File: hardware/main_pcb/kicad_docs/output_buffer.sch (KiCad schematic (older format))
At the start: 4 parts, among them U1 TL072

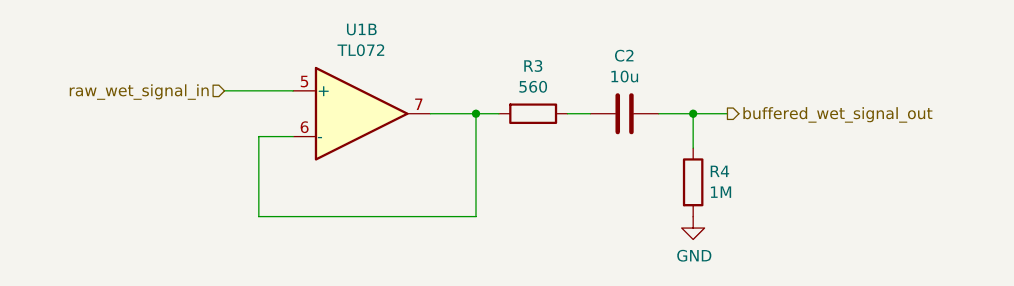
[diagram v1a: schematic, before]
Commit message: flip env invert switch, condense cap types
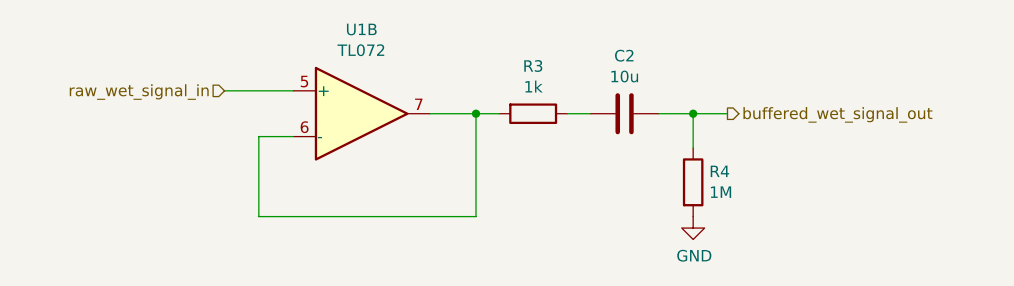
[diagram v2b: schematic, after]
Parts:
- R3: value 560 -> 1k
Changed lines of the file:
@@
 P 6300 3750
 F 0 "R3" V 6093 3750 50  0000 C CNN
-F 1 "560" V 6184 3750 50  0000 C CNN
+F 1 "1k" V 6184 3750 50  0000 C CNN
 F 2 "Resistor_SMD:R_0805_2012Metric" V 6230 3750 50  0001 C CNN
 F 3 "~" H 6300 3750 50  0001 C CNN

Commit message: center envelope follower around +1v, tidy up
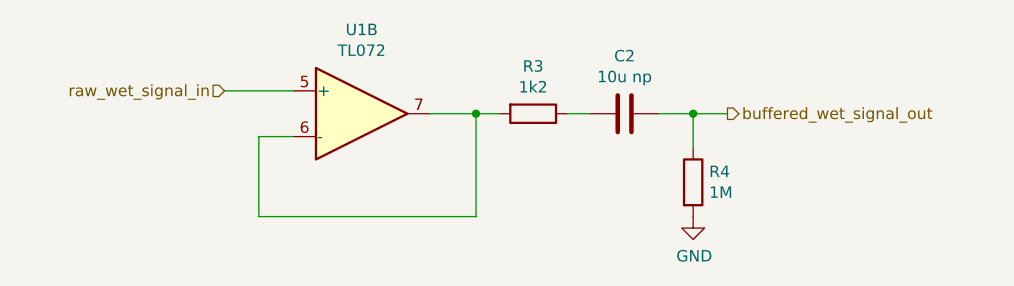
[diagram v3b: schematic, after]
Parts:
- C2: value 10u -> 10u np
- R3: value 1k -> 1k2
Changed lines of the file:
@@
 Sheet 3 8
 Title "Whooshy Sound Filter Pedal"
-Date "2021-06-29"
-Rev "0"
+Date "2021-08-05"
+Rev "0.1"
 Comp ""
 Comment1 "creativecommons.org/licenses/by/4.0/"
@@
 P 6700 3750
 F 0 "C2" V 6448 3750 50  0000 C CNN
-F 1 "10u" V 6539 3750 50  0000 C CNN
+F 1 "10u np" V 6539 3750 50  0000 C CNN
 F 2 "Capacitor_THT:C_Radial_D6.3mm_H11.0mm_P2.50mm" H 6738 3600 50  0001 C CNN
 F 3 "~" H 6700 3750 50  0001 C CNN
@@
 P 6300 3750
 F 0 "R3" V 6093 3750 50  0000 C CNN
-F 1 "1k" V 6184 3750 50  0000 C CNN
+F 1 "1k2" V 6184 3750 50  0000 C CNN
 F 2 "Resistor_SMD:R_0805_2012Metric" V 6230 3750 50  0001 C CNN
 F 3 "~" H 6300 3750 50  0001 C CNN
